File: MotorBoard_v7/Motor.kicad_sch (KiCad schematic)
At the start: 15 parts, among them J7 Servo, J8 Right, J9 Left, U7 DRV8871DDAR, U8 DRV8871DDAR

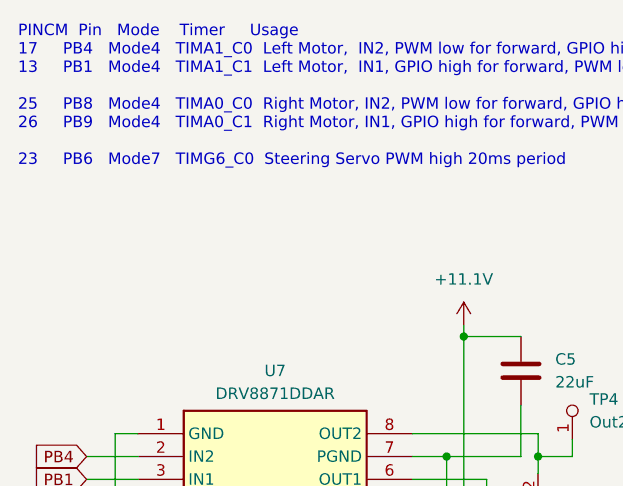
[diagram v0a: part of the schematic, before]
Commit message: added lab 6 update starter files
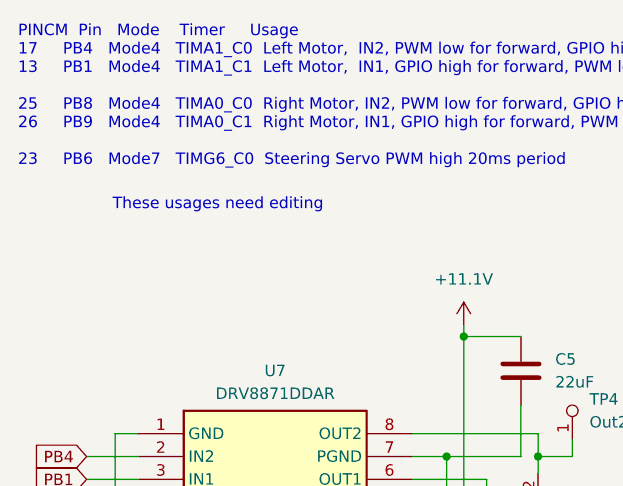
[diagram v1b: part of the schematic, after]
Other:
- note added: "These usages need editing"
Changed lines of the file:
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@@
 	(title_block
 		(title "ECE445M Robot Board")
-		(date "2025-12-23")
-		(rev "v7")
+		(date "2026-01-24")
+		(rev "v7.1")
 		(company "The University of Texas at Austin")
 		(comment 1 "Jonathan Valvano")
@@
 		)
 	)
+	(text "These usages need editing"
+		(exclude_from_sim no)
+		(at 43.18 36.195 0)
+		(effects
+			(font
+				(size 1.27 1.27)
+			)
+		)
+	)
